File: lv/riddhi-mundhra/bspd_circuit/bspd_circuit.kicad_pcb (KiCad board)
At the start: 2 copper layers, 4 parts, among them U1 OPA196xDGK, U2 OPA196xDGK, U3 TLV172IDCK

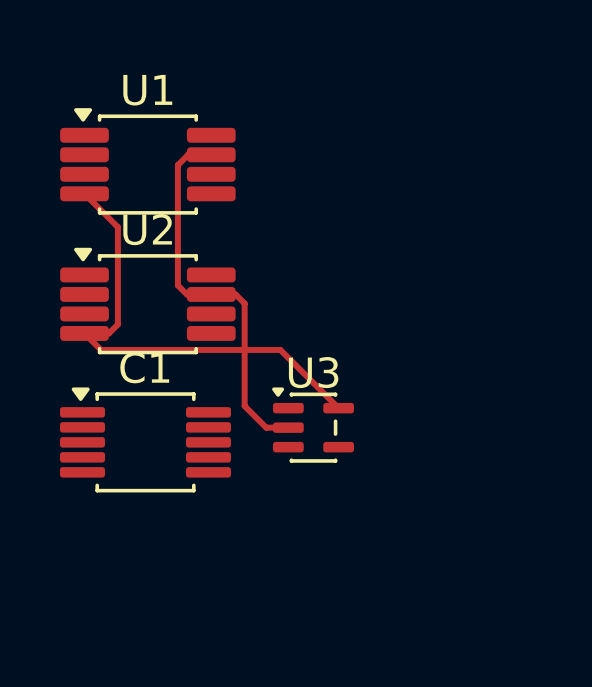
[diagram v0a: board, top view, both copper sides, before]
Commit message: update schematic
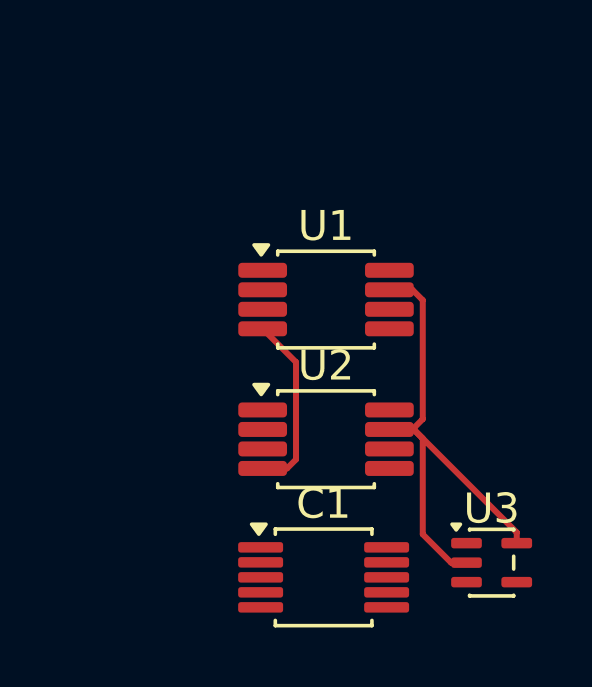
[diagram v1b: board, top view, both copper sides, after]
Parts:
- moved C1 7.45 mm to (122.6, 108.6)
- moved U1 7.45 mm to (122.6, 99.4)
- moved U2 7.45 mm to (122.6, 104.0)
- moved U3 7.45 mm to (128.2, 108.2)
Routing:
- net +3V3: track 28.5 -> 24.0 mm
